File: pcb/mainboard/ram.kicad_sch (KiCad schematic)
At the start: 35 parts

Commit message: Mainboard schematics WIP
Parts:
- gave numbers to parts that had none: 33
- renumbered C420 to C301, C422 to C304

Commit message: Draft motherboard schematics for r0.0 layout
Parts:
- C313, C314, C315, C316, C317, C318, C319, C320, C321, C322, C323, C324, C325, C326: footprint Capacitor_SMD:C_0402_1005Metric -> Capacitor_SMD:C_0201_0603Metric
- TP301, TP302: footprint (none) -> TestPoint:TestPoint_Pad_D1.0mm
- U302: renamed from U303; value IS43LQ32256A-062BLI -> MT53D512M16D1DS-046
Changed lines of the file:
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@@
       (effects (font (size 1.27 1.27)) (justify left))
     )
-    (property "Footprint" "Capacitor_SMD:C_0402_1005Metric" (id 2) (at 254.9652 139.7 0)
+    (property "Footprint" "Capacitor_SMD:C_0201_0603Metric" (id 2) (at 254.9652 139.7 0)
       (effects (font (size 1.27 1.27)) hide)
     )
@@
       (effects (font (size 1.27 1.27)) hide)
     )
-    (property "Footprint" "" (id 2) (at 45.72 162.56 0)
+    (property "Footprint" "TestPoint:TestPoint_Pad_D1.0mm" (id 2) (at 45.72 162.56 0)
       (effects (font (size 1.27 1.27)) hide)
     )
@@
       (effects (font (size 1.27 1.27)) (justify left))
     )
-    (property "Footprint" "Capacitor_SMD:C_0402_1005Metric" (id 2) (at 254.9652 157.48 0)
+    (property "Footprint" "Capacitor_SMD:C_0201_0603Metric" (id 2) (at 254.9652 157.48 0)
       (effects (font (size 1.27 1.27)) hide)
     )
@@
       (effects (font (size 1.27 1.27)) (justify left))
     )
-    (property "Footprint" "Capacitor_SMD:C_0402_1005Metric" (id 2) (at 229.5652 139.7 0)
+    (property "Footprint" "Capacitor_SMD:C_0201_0603Metric" (id 2) (at 229.5652 139.7 0)
       (effects (font (size 1.27 1.27)) hide)
     )
@@
       (effects (font (size 1.27 1.27)) (justify left))
     )
-    (property "Footprint" "Capacitor_SMD:C_0402_1005Metric" (id 2) (at 216.8652 121.92 0)
+    (property "Footprint" "Capacitor_SMD:C_0201_0603Metric" (id 2) (at 216.8652 121.92 0)
       (effects (font (size 1.27 1.27)) hide)
     )
@@
       (effects (font (size 1.27 1.27)) (justify left))
     )
-    (property "Footprint" "Capacitor_SMD:C_0402_1005Metric" (id 2) (at 229.5652 157.48 0)
+    (property "Footprint" "Capacitor_SMD:C_0201_0603Metric" (id 2) (at 229.5652 157.48 0)
       (effects (font (size 1.27 1.27)) hide)
     )
@@
       (effects (font (size 1.27 1.27)) hide)
     )
-    (property "Footprint" "" (id 2) (at 45.72 172.72 0)
+    (property "Footprint" "TestPoint:TestPoint_Pad_D1.0mm" (id 2) (at 45.72 172.72 0)
       (effects (font (size 1.27 1.27)) hide)
     )
@@
       (effects (font (size 1.27 1.27)) (justify left))
     )
-    (property "Footprint" "Capacitor_SMD:C_0402_1005Metric" (id 2) (at 204.1652 121.92 0)
+    (property "Footprint" "Capacitor_SMD:C_0201_0603Metric" (id 2) (at 204.1652 121.92 0)
       (effects (font (size 1.27 1.27)) hide)
     )
@@
       (effects (font (size 1.27 1.27)) (justify left))
     )
-    (property "Footprint" "Capacitor_SMD:C_0402_1005Metric" (id 2) (at 242.2652 139.7 0)
+    (property "Footprint" "Capacitor_SMD:C_0201_0603Metric" (id 2) (at 242.2652 139.7 0)
       (effects (font (size 1.27 1.27)) hide)
     )
@@
       (effects (font (size 1.27 1.27)) (justify left))
     )
-    (property "Footprint" "Capacitor_SMD:C_0402_1005Metric" (id 2) (at 204.1652 139.7 0)
+    (property "Footprint" "Capacitor_SMD:C_0201_0603Metric" (id 2) (at 204.1652 139.7 0)
       (effects (font (size 1.27 1.27)) hide)
     )
@@
       (effects (font (size 1.27 1.27)) (justify left))
     )
-    (property "Footprint" "Capacitor_SMD:C_0402_1005Metric" (id 2) (at 204.1652 157.48 0)
+    (property "Footprint" "Capacitor_SMD:C_0201_0603Metric" (id 2) (at 204.1652 157.48 0)
       (effects (font (size 1.27 1.27)) hide)
     )
@@
       (effects (font (size 1.27 1.27)) (justify left))
     )
-    (property "Footprint" "Capacitor_SMD:C_0402_1005Metric" (id 2) (at 229.5652 121.92 0)
+    (property "Footprint" "Capacitor_SMD:C_0201_0603Metric" (id 2) (at 229.5652 121.92 0)
       (effects (font (size 1.27 1.27)) hide)
     )
@@
   (symbol (lib_id "Memory_RAM:IS43LQ32256A-062BLI") (at 243.84 66.04 0) (unit 2)
     (in_bom yes) (on_board yes) (fields_autoplaced)
-    (property "Reference" "U303" (id 0) (at 245.8594 101.6 0)
-      (effects (font (size 1.27 1.27)) (justify left))
-    )
-    (property "Value" "IS43LQ32256A-062BLI" (id 1) (at 245.8594 104.14 0)
+    (property "Reference" "U302" (id 0) (at 245.8594 101.6 0)
+      (effects (font (size 1.27 1.27)) (justify left))
+    )
+    (property "Value" "MT53D512M16D1DS-046" (id 1) (at 245.8594 104.14 0)
       (effects (font (size 1.27 1.27)) (justify left))
     )
@@
       (effects (font (size 1.27 1.27)) (justify left))
     )
-    (property "Footprint" "Capacitor_SMD:C_0402_1005Metric" (id 2) (at 216.8652 157.48 0)
+    (property "Footprint" "Capacitor_SMD:C_0201_0603Metric" (id 2) (at 216.8652 157.48 0)
       (effects (font (size 1.27 1.27)) hide)
     )
@@
       (effects (font (size 1.27 1.27)) (justify left))
     )
-    (property "Footprint" "Capacitor_SMD:C_0402_1005Metric" (id 2) (at 242.2652 157.48 0)
+    (property "Footprint" "Capacitor_SMD:C_0201_0603Metric" (id 2) (at 242.2652 157.48 0)
       (effects (font (size 1.27 1.27)) hide)
     )
@@
       (effects (font (size 1.27 1.27)) (justify left))
     )
-    (property "Footprint" "Capacitor_SMD:C_0402_1005Metric" (id 2) (at 242.2652 121.92 0)
+    (property "Footprint" "Capacitor_SMD:C_0201_0603Metric" (id 2) (at 242.2652 121.92 0)
       (effects (font (size 1.27 1.27)) hide)
     )
@@
       (effects (font (size 1.27 1.27)) (justify left))
     )
-    (property "Footprint" "Capacitor_SMD:C_0402_1005Metric" (id 2) (at 216.8652 139.7 0)
-      (effects (font (size 1.27 1.27)) hide)
-    )
+    (property "Footprint" "Capacitor_SMD:C_0201_0603Metric" (id 2) (at 216.8652 139.7 0)
+      (effects (font (size 1.27 1.27)) hide)
+    )

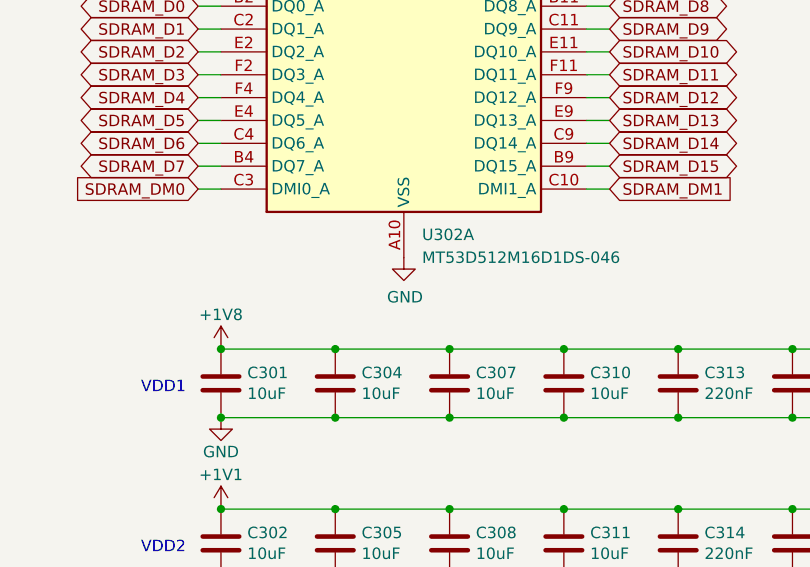
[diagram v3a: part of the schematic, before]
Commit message: Motherboard PCB component initial placement, schematics fixes
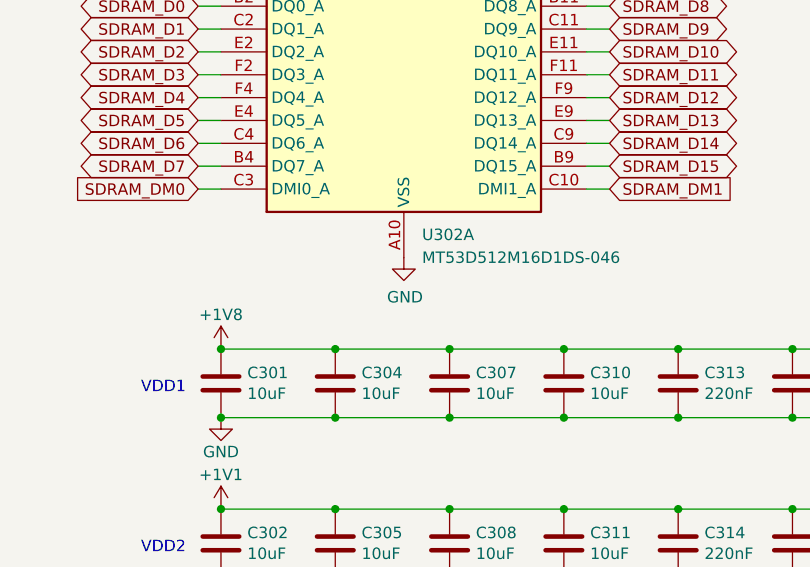
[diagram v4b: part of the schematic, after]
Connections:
- net GND: now also U302.A10 (VSS), U302.A3 (VSS), U302.C1 (VSS), U302.C12 (VSS), U302.C5 (VSS), U302.C8 (VSS), U302.D11 (VSS), U302.D2 (VSS), U302.D4 (VSS), U302.D9 (VSS), U302.E1 (VSS), U302.E12 (VSS), U302.E5 (VSS), U302.E8 (VSS), U302.G1 (VSS), U302.G10 (VSS), U302.G12 (VSS), U302.G3 (VSS), U302.G5 (VSS), U302.G8 (VSS), U302.J1 (VSS), U302.J10 (VSS), U302.J12 (VSS), U302.J3 (VSS), U302.K11 (VSS), U302.K2 (VSS), U302.K4 (VSS), U302.K9 (VSS)
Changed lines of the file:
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@@
     (pin "2")
   )
-  (symbol (lib_id "power:GND") (at 172.72 104.1401 0) (unit 1)
+  (symbol (lib_id "power:GND") (at 172.72 104.14 0) (unit 1)
     (in_bom yes) (on_board yes)
-    (property "Reference" "#PWR0310" (id 0) (at 172.72 110.4901 0)
+    (property "Reference" "#PWR0310" (id 0) (at 172.72 110.49 0)
       (effects (font (size 1.27 1.27)) hide)
     )
-    (property "Value" "GND" (id 1) (at 172.847 108.5343 0))
-    (property "Footprint" "" (id 2) (at 172.72 104.1401 0)
+    (property "Value" "GND" (id 1) (at 172.847 108.5342 0))
+    (property "Footprint" "" (id 2) (at 172.72 104.14 0)
       (effects (font (size 1.27 1.27)) hide)
     )
-    (property "Datasheet" "" (id 3) (at 172.72 104.1401 0)
+    (property "Datasheet" "" (id 3) (at 172.72 104.14 0)
       (effects (font (size 1.27 1.27)) hide)
     )

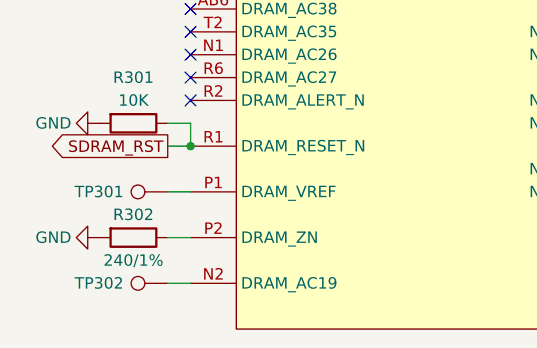
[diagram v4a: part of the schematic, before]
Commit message: Routing mainboard in progress, schematics fixes
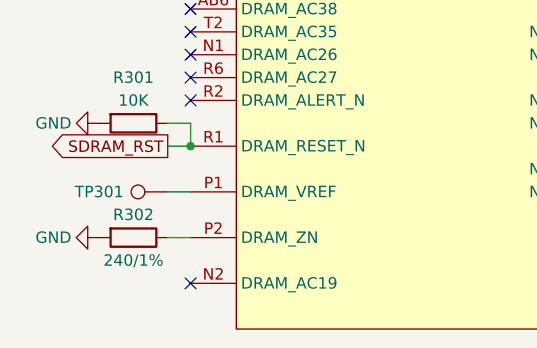
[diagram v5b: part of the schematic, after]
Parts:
- removed TP302: TestPoint, TestPoint:TestPoint_Pad_D1.0mm, symbol Connector:TestPoint
- U302: footprint Package_BGA:BGA-200_10.0x14.5mm_Layout12x22_P0.80x0.65mm -> footprint:BGA-200_10.0x14.5mm_Layout12x22_P0.80x0.65mm_B0.3mm
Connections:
- no-connect marks 81 -> 82
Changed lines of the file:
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@@
   (no_connect (at 93.98 121.92))
   (no_connect (at 93.98 139.7))
+  (no_connect (at 48.26 177.8))
   (no_connect (at 48.26 144.78))
   (no_connect (at 264.16 88.9))
@@
     (stroke (width 0) (type default) (color 0 0 0 0))
   )
-  (wire (pts (xy 45.72 177.8) (xy 48.26 177.8))
-    (stroke (width 0) (type default) (color 0 0 0 0))
-  )
   (wire (pts (xy 246.38 25.4) (xy 246.38 27.94))
     (stroke (width 0) (type default) (color 0 0 0 0))
@@
     (pin "1")
     (pin "2")
-  )
-  (symbol (lib_id "Connector:TestPoint") (at 45.72 177.8 90) (unit 1)
-    (in_bom yes) (on_board yes)
-    (property "Reference" "TP302" (id 0) (at 38.1 177.8 90))
-    (property "Value" "TestPoint" (id 1) (at 35.56 179.07 90)
-      (effects (font (size 1.27 1.27)) hide)
-    )
-    (property "Footprint" "TestPoint:TestPoint_Pad_D1.0mm" (id 2) (at 45.72 172.72 0)
-      (effects (font (size 1.27 1.27)) hide)
-    )
-    (property "Datasheet" "~" (id 3) (at 45.72 172.72 0)
-      (effects (font (size 1.27 1.27)) hide)
-    )
-    (pin "1")
   )
   (symbol (lib_id "power:GND") (at 152.4 139.7 0) (unit 1)
@@
       (effects (font (size 1.27 1.27)) (justify left))
     )
-    (property "Footprint" "Package_BGA:BGA-200_10.0x14.5mm_Layout12x22_P0.80x0.65mm" (id 2) (at 173.99 114.3 0)
+    (property "Footprint" "footprint:BGA-200_10.0x14.5mm_Layout12x22_P0.80x0.65mm_B0.3mm" (id 2) (at 173.99 114.3 0)
       (effects (font (size 1.27 1.27)) hide)
     )
@@
       (effects (font (size 1.27 1.27)) (justify left))
     )
-    (property "Footprint" "Package_BGA:BGA-200_10.0x14.5mm_Layout12x22_P0.80x0.65mm" (id 2) (at 245.11 114.3 0)
-      (effects (font (size 1.27 1.27)) hide)
-    )
+    (property "Footprint" "footprint:BGA-200_10.0x14.5mm_Layout12x22_P0.80x0.65mm_B0.3mm" (id 2) (at 245.11 114.3 0)
+      (effects (font (size 1.27 1.27)) hide)
+    )
